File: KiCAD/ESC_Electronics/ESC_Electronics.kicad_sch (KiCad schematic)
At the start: 70 parts, among them J1 -1000VDC, J2 Test Input, J3 CA probe, J4 DC Power, J5 Output, J6 Barrel_Jack, J7 -6V, J8 +6V, J9 Batt probe, Q1 MMBT3906, Q2 MMBT3904, U1 CR110, U2 SiPhotodiode, U3 TL072, U4 LM317, U5 TLE2426xP

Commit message: published as V2 on OSHPark
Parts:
- removed C11, C12: 10uF, Capacitor_SMD:C_0805_2012Metric_Pad1.18x1.45mm_HandSolder, symbol Device:C_Small
- removed D1, D2: RB751V-40, Diode_SMD:D_SOD-323_HandSoldering, symbol Device:D_Schottky
- removed D5, D6: MM3Z7V5T1G, Diode_SMD:D_SOD-323_HandSoldering, symbol Diode:MM3Zxx
- removed Q1: MMBT3906, Package_TO_SOT_SMD:SOT-23, symbol Transistor_BJT:MMBT3906
- removed Q2: MMBT3904, Package_TO_SOT_SMD:SOT-23, symbol Transistor_BJT:MMBT3904
- removed R12: 10k, Resistor_THT:R_Axial_DIN0207_L6.3mm_D2.5mm_P10.16mm_Horizontal, symbol Device:R_Small_US
- removed R16, R17: 1k, Resistor_SMD:R_0805_2012Metric_Pad1.20x1.40mm_HandSolder, symbol Device:R_Small_US
- removed R18, R19: 20, Resistor_SMD:R_1206_3216Metric_Pad1.30x1.75mm_HandSolder, symbol Device:R_Small_US
- removed R2, R7: 4.7, Resistor_SMD:R_2512_6332Metric_Pad1.40x3.35mm_HandSolder, symbol Device:R_Small_US
- removed R6: 0, Resistor_THT:R_Axial_DIN0207_L6.3mm_D2.5mm_P10.16mm_Horizontal, symbol Device:R_Small_US
- added C13, C14: 0.33uF, Capacitor_SMD:C_0805_2012Metric_Pad1.18x1.45mm_HandSolder, symbol Device:C_Small
- added C15, C16: 100nF, Capacitor_SMD:C_0805_2012Metric_Pad1.18x1.45mm_HandSolder, symbol Device:C_Small
- added C17, C18: 0.1uF, Capacitor_SMD:C_0805_2012Metric_Pad1.18x1.45mm_HandSolder, symbol Device:C_Small
- added C8: open, Capacitor_SMD:C_0805_2012Metric_Pad1.18x1.45mm_HandSolder, symbol Device:C_Small
- added FB1, FB2: FerriteBead_Small, Inductor_SMD:L_1206_3216Metric_Pad1.22x1.90mm_HandSolder, symbol Device:FerriteBead_Small
- added J10: RV Prob, Connector_PinHeader_2.54mm:PinHeader_1x02_P2.54mm_Vertical, symbol Connector:Conn_01x02_Male
- added R10: 750, Resistor_SMD:R_0805_2012Metric_Pad1.20x1.40mm_HandSolder, symbol Device:R_Small_US
- added RV1: 10k, Potentiometer_THT:Potentiometer_Bourns_3266W_Vertical, symbol Device:R_Potentiometer_US
- added U5: UA78M08, Package_TO_SOT_SMD:SOT-223-3_TabPin2, symbol Regulator_Linear:uA7808
- added U6: UA79M08, Package_TO_SOT_SMD:TO-252-3_TabPin2, symbol Regulator_Linear:uA7808
- C3: footprint Capacitor_THT:C_Disc_D10.5mm_W5.0mm_P7.50mm -> Capacitor_THT:C_Disc_D10.5mm_W5.0mm_P10.00mm
- C6: renamed from C7; footprint Capacitor_THT:C_Disc_D14.5mm_W5.0mm_P7.50mm -> Capacitor_THT:C_Disc_D12.5mm_W5.0mm_P10.00mm
- C7: renamed from C5; footprint Capacitor_THT:C_Disc_D10.5mm_W5.0mm_P7.50mm -> Capacitor_THT:C_Disc_D10.5mm_W5.0mm_P10.00mm
- J6: footprint Connector_Wire:SolderWire-0.5sqmm_1x02_P4.6mm_D0.9mm_OD2.1mm -> Connector_PinHeader_2.54mm:PinHeader_1x02_P2.54mm_Vertical
- J7: renamed from J4; footprint TerminalBlock_4Ucon:TerminalBlock_4Ucon_1x03_P3.50mm_Vertical -> Connector_PinHeader_2.54mm:PinHeader_1x03_P2.54mm_Vertical
- J8: renamed from J7; value -6V -> -8V
- J9: renamed from J8; value +6V -> +8V
- R11: renamed from R20; value 10k -> 20k; footprint Resistor_THT:R_Axial_DIN0207_L6.3mm_D2.5mm_P10.16mm_Horizontal -> Resistor_SMD:R_0805_2012Metric_Pad1.20x1.40mm_HandSolder
- R13: renamed from R14; value 2.94k -> 7k
- R14: renamed from R15; value 220 -> 470
- R2: renamed from R3; footprint Resistor_THT:R_Axial_DIN0207_L6.3mm_D2.5mm_P10.16mm_Horizontal -> Resistor_THT:R_Axial_DIN0207_L6.3mm_D2.5mm_P15.24mm_Horizontal
- R3: renamed from R4; footprint Resistor_THT:R_Axial_DIN0207_L6.3mm_D2.5mm_P10.16mm_Horizontal -> Resistor_THT:R_Axial_DIN0207_L6.3mm_D2.5mm_P15.24mm_Horizontal
- R4: renamed from R5; footprint Resistor_THT:R_Axial_DIN0207_L6.3mm_D2.5mm_P10.16mm_Horizontal -> Resistor_THT:R_Axial_DIN0207_L6.3mm_D2.5mm_P15.24mm_Horizontal
- R6: renamed from R8; footprint Resistor_THT:R_Axial_DIN0207_L6.3mm_D2.5mm_P10.16mm_Horizontal -> Resistor_THT:R_Axial_DIN0207_L6.3mm_D2.5mm_P15.24mm_Horizontal
- R8: renamed from R9; footprint Resistor_THT:R_Axial_DIN0207_L6.3mm_D2.5mm_P7.62mm_Horizontal -> Resistor_THT:R_Axial_DIN0207_L6.3mm_D2.5mm_P15.24mm_Horizontal
- R9: renamed from R11; value 1k -> 0; footprint Resistor_THT:R_Axial_DIN0207_L6.3mm_D2.5mm_P10.16mm_Horizontal -> Resistor_SMD:R_1206_3216Metric_Pad1.30x1.75mm_HandSolder
- U3: value TL072 -> TL051CP
- U4: value LM317 -> LM317L; footprint Package_TO_SOT_THT:TO-220-3_Horizontal_TabDown -> Package_TO_SOT_SMD:SOT-89-3_Handsoldering; Digikey 497-19621-ND -> 296-50352-1-ND
- U7: renamed from U5; footprint Package_TO_SOT_THT:TO-92L_Inline_Wide -> Package_SO:SOIC-8_3.9x4.9mm_P1.27mm; symbol Reference_Voltage:TLE2426xP -> Reference_Voltage:TLE2426xD
- renumbered C9 to C10, C8 to C11, C10 to C12, C6 to C5, C13 to C9, D3 to D1, D4 to D2, J9 to J1, J3 to J2, J2 to J3, J1 to J4, R13 to R12, R10 to R7
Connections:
- net GND: now also J2.1 (Pin_1), C13.2, C14.2, C16.2, C17.2, C18.2, C8.2, J10.2 (Pin_2), RV1.2, U5.2 (GND), U6.2 (GND); no longer J2.2 (Pin_2)
- net at R11.1, U3.2 (1IN-): now also R10.2
- net at D1.1 (K): now also J7.3 (Pin_3), C13.1, U5.1 (IN)
- net at U1.5 (-Vs): now also C4.1, FB2.1
- net at J7.1 (Pin_1): now also D2.2 (A), C14.1, U6.1 (IN)
- net at U1.6 (+Vs): now also C1.1, FB1.1
- net at R9.1, U1.8 (output): now also J2.2 (Pin_2); no longer J2.1 (Pin_1)
- net at R2.2, R4.1, R8.1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: now also C3.2
- net at C12.1, D1.2 (A), R14.1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: now also C15.1
- net at R9.2, U3.3 (1IN+): now also C8.1
- net at U7.8 (NOISE_REDUCTION): now also C15.2, C16.1
- net +6VDC renamed +8VDC
- net +8VDC: now also C17.1, FB1.2, U5.3 (OUT); no longer C1.1
- net -6VDC renamed -8VDC
- net -8VDC: now also C18.1, FB2.2, U6.3 (OUT); no longer C4.1
- new net: J10.1 (Pin_1), R10.1, RV1.1
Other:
- note added: "-10V"
- note added: "20V"
- note added: "A = 1+Rf/R2"
- note added: "R2=RV+R10"
- note added: "Rf"
- note added: "Vout = 1.25(1+R15/R14)"
- note removed: "18V"
- note removed: "A = 1+R20/R12"
- moved on the sheet: BT1, BT2, BT3, BT4, BT5, BT6, C1, C10, C11, C12, C2, C3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

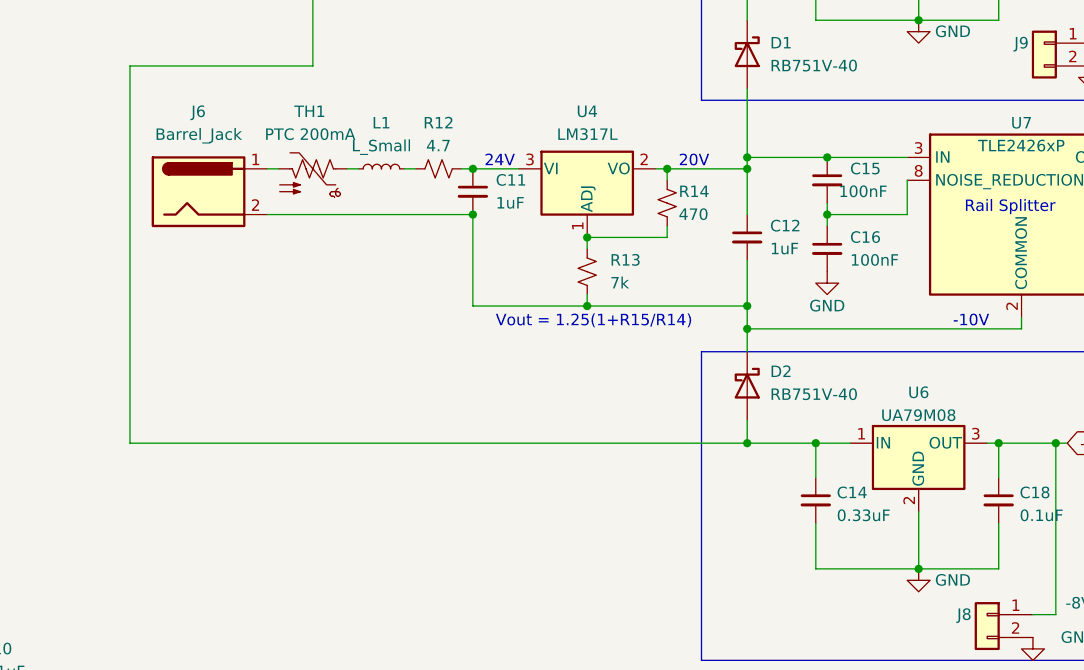
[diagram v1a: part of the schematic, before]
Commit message: fixed U6 pad and updated several footprints to latest KiCAD versions
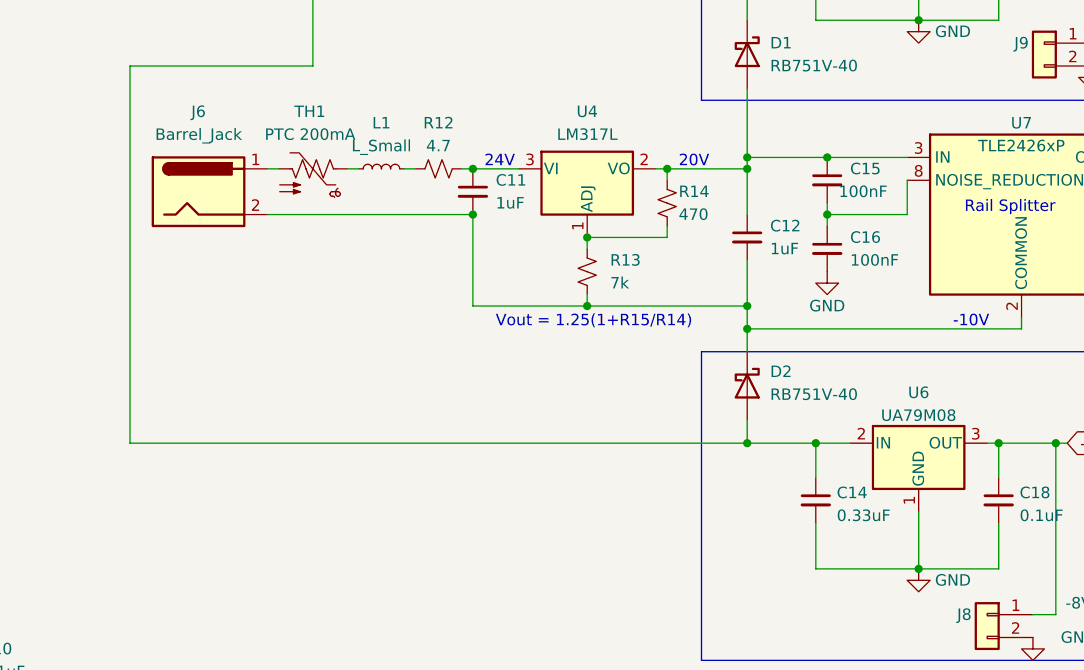
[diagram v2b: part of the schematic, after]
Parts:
- U6: footprint Package_TO_SOT_SMD:TO-252-3_TabPin2 -> ESC_Electronics_Library:TO-252-3_Tab1
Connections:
- net GND: now also U6.1 (GND); no longer U6.2 (GND)
- net at C14.1, D2.2 (A), J7.1 (Pin_1): now also U6.2 (IN); no longer U6.1 (IN)

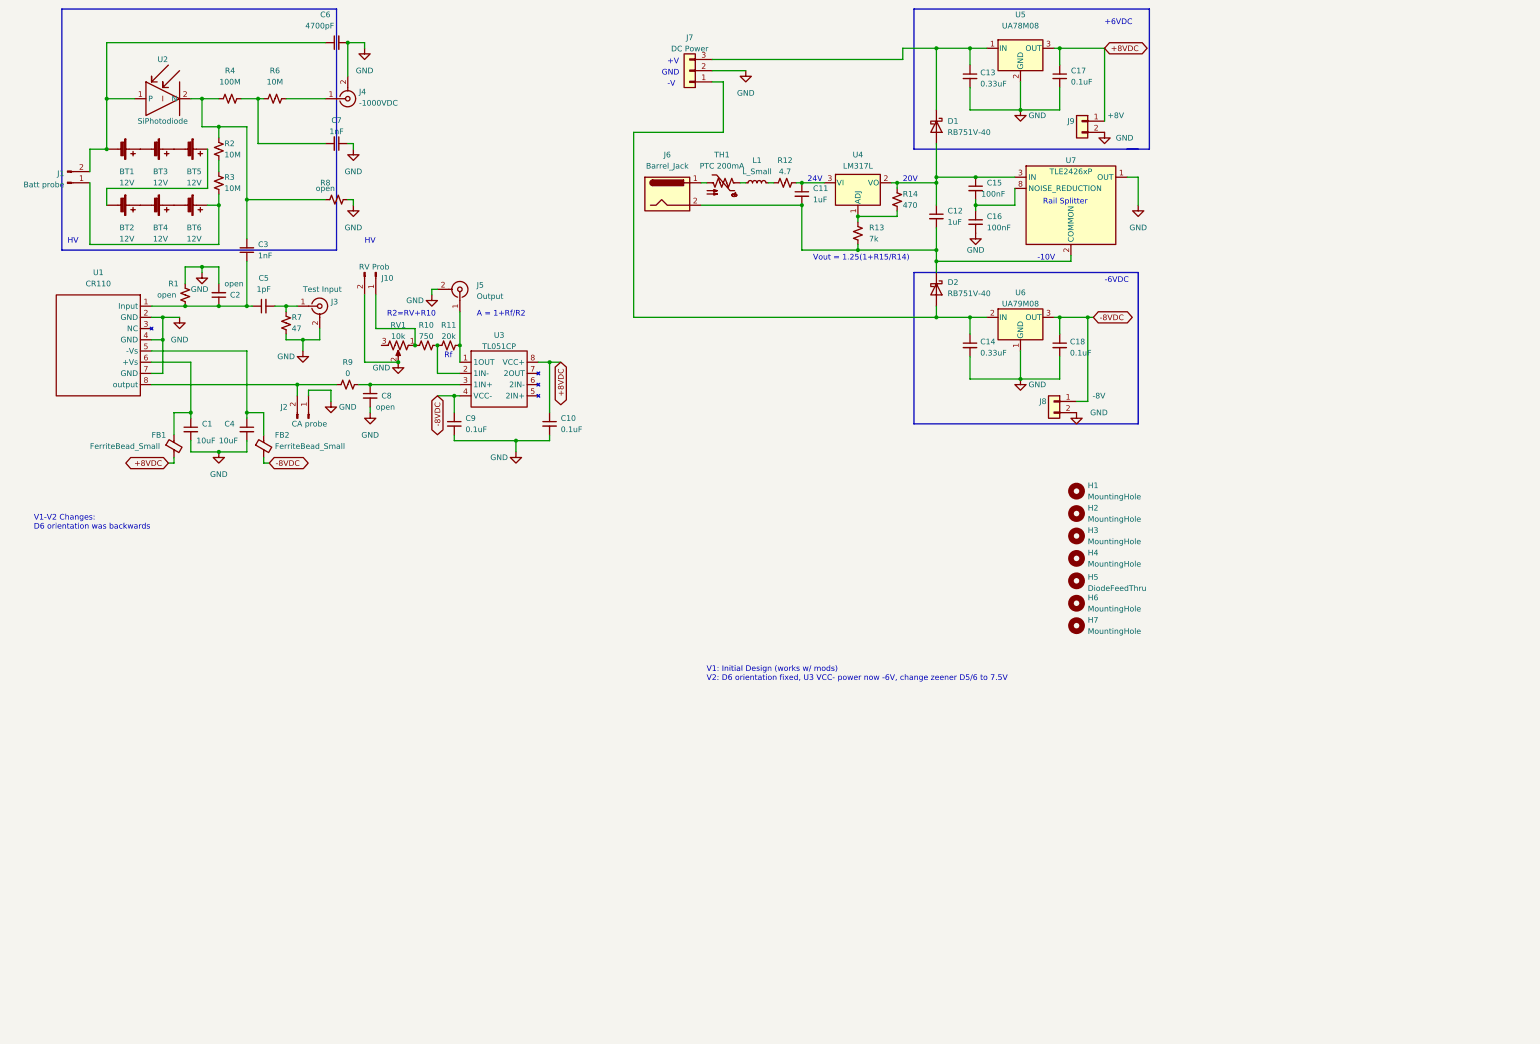
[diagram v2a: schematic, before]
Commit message: Updating Digikey Partnumbers
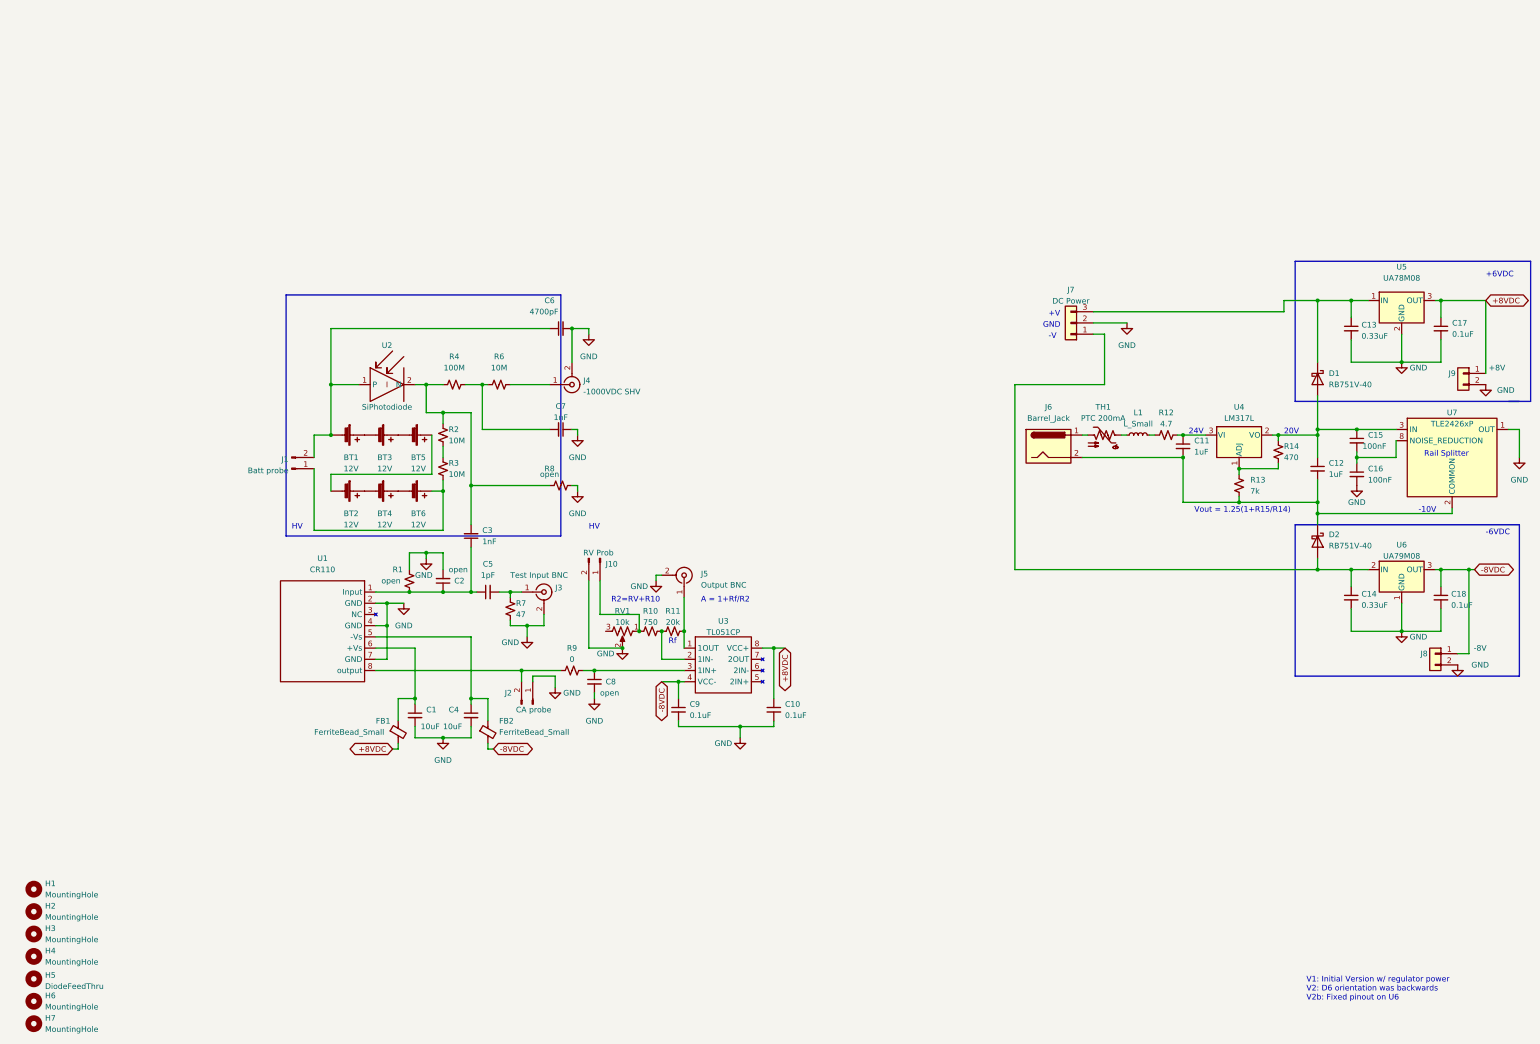
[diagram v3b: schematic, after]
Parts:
- J1, J2, J7: Digikey (none) -> N/A
- J3: value Test Input -> Test Input BNC
- J4: value -1000VDC -> -1000VDC SHV; Digikey 2737-RHV-116-ND -> 4912-SHV-BR-ND
- J5: value Output -> Output BNC
- R2: Digikey HVA05FA10M0CT-ND -> HVA12FA10M0CT-ND
- R4: Digikey HVA05FA100MCT-ND -> HVA12FA100MCT-ND
- R6: Digikey HVA05FA10M0CT-ND -> HVA12FA10M0
- R9: Digikey RNCP0805FTD1K00CT-ND -> RMCF0805ZT0R00
- RV1: Digikey (none) -> 3266W-103LF-ND
- U1: Digikey (none) -> ED11161-ND
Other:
- note added: "V1: Initial Version w/ regulator power V2: D6 orientation was backwards V2b: Fixed pinout on U6"
- note removed: "V1-V2 Changes: D6 orientation was backwards"
- note removed: "V1: Initial Design (works w/ mods) V2: D6 orientation fixed, U3 VCC- power now -6V, change zeener D5/6 to 7.5V"
- company: (none) -> ESC
- title: (none) -> ESC Electronics
- moved on the sheet: BT1, BT2, BT3, BT4, BT5, BT6, C1, C10, C11, C12, C13, C14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
